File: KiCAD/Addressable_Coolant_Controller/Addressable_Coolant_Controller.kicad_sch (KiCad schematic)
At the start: 3 parts, among them J10 XW4M-12D2-H1DA, J11 XW4M-12D2-H1DA, J12 XW4M-02D1-H1DA

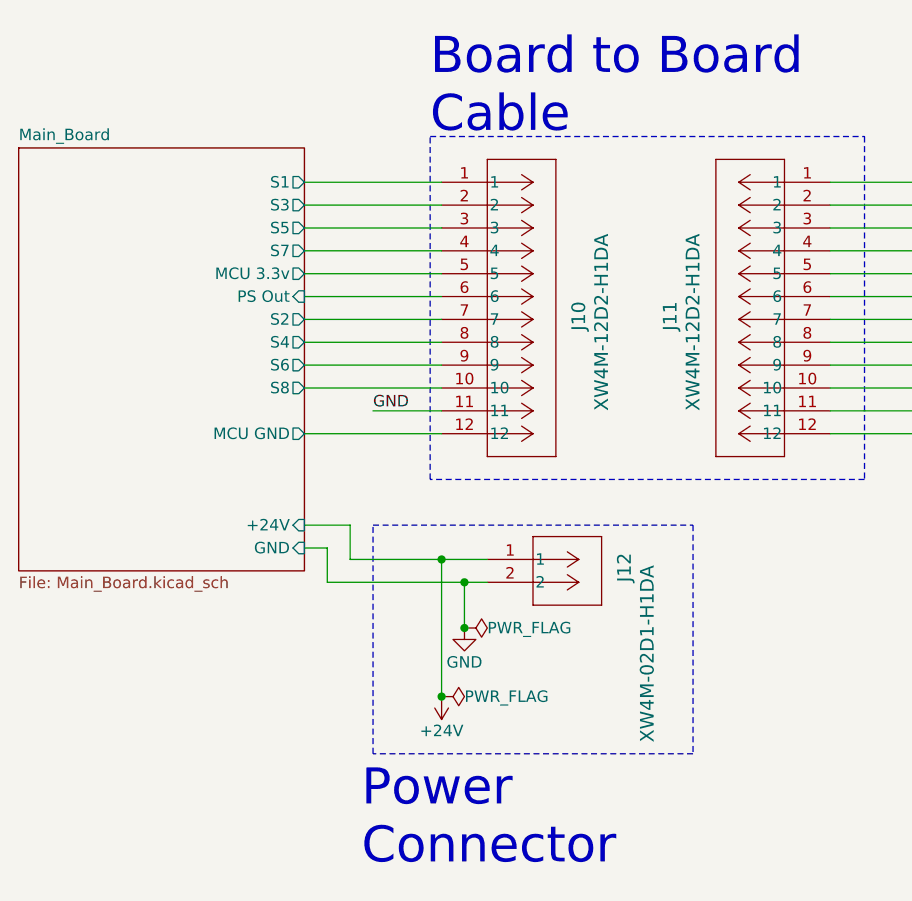
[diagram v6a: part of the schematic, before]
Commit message: Added LEDs to connector board, and moved to hierarchical sheet
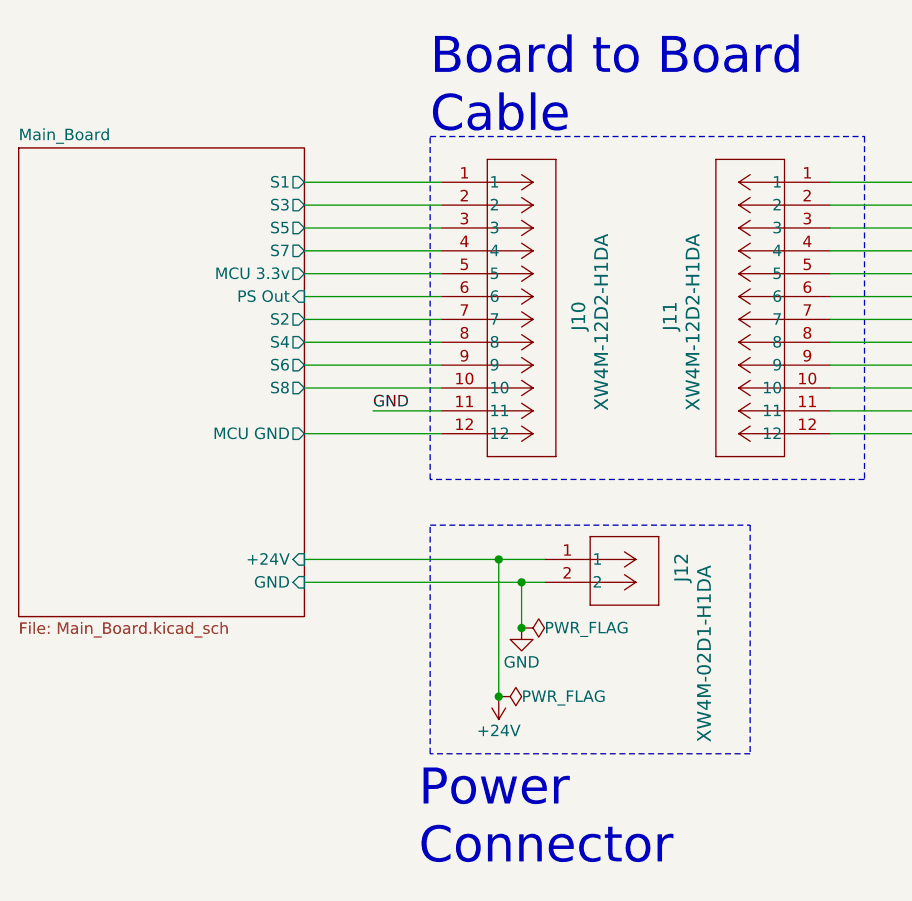
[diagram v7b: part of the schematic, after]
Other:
- moved on the sheet: J12
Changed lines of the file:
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@@
     (company "Warner Consulting Inc.")
   )
-  (junction (at 127 127) (diameter 0) (color 0 0 0 0)
-  )
-  (junction (at 129.54 114.3) (diameter 0) (color 0 0 0 0)
-  )
-  (junction (at 129.54 119.38) (diameter 0) (color 0 0 0 0)
-  )
-  (junction (at 127 111.76) (diameter 0) (color 0 0 0 0)
+  (junction (at 133.35 127) (diameter 0) (color 0 0 0 0)
+  )
+  (junction (at 135.89 114.3) (diameter 0) (color 0 0 0 0)
+  )
+  (junction (at 135.89 119.38) (diameter 0) (color 0 0 0 0)
+  )
+  (junction (at 133.35 111.76) (diameter 0) (color 0 0 0 0)
   )
   (wire (pts (xy 170.18 90.17) (xy 185.42 90.17))
@@
     (stroke (width 0) (type default))
   )
-  (wire (pts (xy 129.54 119.38) (xy 129.54 114.3))
-    (stroke (width 0) (type default))
-  )
-  (wire (pts (xy 127 111.76) (xy 132.08 111.76))
+  (wire (pts (xy 135.89 119.38) (xy 135.89 114.3))
+    (stroke (width 0) (type default))
+  )
+  (wire (pts (xy 133.35 111.76) (xy 138.43 111.76))
     (stroke (width 0) (type default))
   )
@@
     (stroke (width 0) (type default))
   )
-  (wire (pts (xy 116.84 111.76) (xy 116.84 107.95))
-    (stroke (width 0) (type default))
-  )
   (wire (pts (xy 170.18 69.85) (xy 185.42 69.85))
     (stroke (width 0) (type default))
@@
     (stroke (width 0) (type default))
   )
-  (wire (pts (xy 116.84 107.95) (xy 111.76 107.95))
+  (wire (pts (xy 111.76 111.76) (xy 133.35 111.76))
     (stroke (width 0) (type default))
   )
@@
     (stroke (width 0) (type default))
   )
-  (wire (pts (xy 111.76 110.49) (xy 114.3 110.49))
+  (wire (pts (xy 111.76 114.3) (xy 135.89 114.3))
     (stroke (width 0) (type default))
   )
@@
     (stroke (width 0) (type default))
   )
-  (wire (pts (xy 114.3 110.49) (xy 114.3 114.3))
-    (stroke (width 0) (type default))
-  )
   (wire (pts (xy 170.18 95.25) (xy 185.42 95.25))
     (stroke (width 0) (type default))
   )
-  (wire (pts (xy 116.84 111.76) (xy 127 111.76))
-    (stroke (width 0) (type default))
-  )
-  (wire (pts (xy 129.54 114.3) (xy 132.08 114.3))
+  (wire (pts (xy 135.89 114.3) (xy 138.43 114.3))
     (stroke (width 0) (type default))
   )
@@
     (stroke (width 0) (type default))
   )
-  (wire (pts (xy 114.3 114.3) (xy 129.54 114.3))
-    (stroke (width 0) (type default))
-  )
-  (wire (pts (xy 127 111.76) (xy 127 127))
+  (wire (pts (xy 133.35 111.76) (xy 133.35 127))
     (stroke (width 0) (type default))
   )
@@
     (stroke (width 0) (type default))
   )
-  (rectangle (start 119.38 107.95) (end 154.94 133.35)
+  (rectangle (start 125.73 107.95) (end 161.29 133.35)
     (stroke (width 0) (type dash_dot_dot))
     (fill (type none))
@@
     (effects (font (size 4 4)) (justify left bottom))
   )
-  (text "Power \nConnector" (at 118.11 146.05 0)
+  (text "Power \nConnector" (at 124.46 146.05 0)
     (effects (font (size 4 4)) (justify left bottom))
   )
@@
     (effects (font (size 1.27 1.27)) (justify left bottom))
   )
-  (symbol (lib_id "power:PWR_FLAG") (at 127 127 270) (unit 1)
+  (symbol (lib_id "power:PWR_FLAG") (at 133.35 127 270) (unit 1)
     (in_bom yes) (on_board yes) (dnp no)
-    (property "Reference" "#FLG01" (at 128.905 127 0)
+    (property "Reference" "#FLG01" (at 135.255 127 0)
       (effects (font (size 1.27 1.27)) hide)
     )
-    (property "Value" "PWR_FLAG" (at 129.54 127 90)
+    (property "Value" "PWR_FLAG" (at 135.89 127 90)
       (effects (font (size 1.27 1.27)) (justify left))
     )
-    (property "Footprint" "" (at 127 127 0)
+    (property "Footprint" "" (at 133.35 127 0)
       (effects (font (size 1.27 1.27)) hide)
     )
-    (property "Datasheet" "~" (at 127 127 0)
+    (property "Datasheet" "~" (at 133.35 127 0)
       (effects (font (size 1.27 1.27)) hide)
     )
@@
     )
   )
-  (symbol (lib_id "power:GND") (at 129.54 119.38 0) (unit 1)
+  (symbol (lib_id "power:GND") (at 135.89 119.38 0) (unit 1)
     (in_bom yes) (on_board yes) (dnp no)
-    (property "Reference" "#PWR02" (at 129.54 125.73 0)
+    (property "Reference" "#PWR02" (at 135.89 125.73 0)
       (effects (font (size 1.27 1.27)) hide)
     )
-    (property "Value" "GND" (at 129.54 123.19 0)
+    (property "Value" "GND" (at 135.89 123.19 0)
       (effects (font (size 1.27 1.27)))
     )
-    (property "Footprint" "" (at 129.54 119.38 0)
+    (property "Footprint" "" (at 135.89 119.38 0)
       (effects (font (size 1.27 1.27)) hide)
     )
-    (property "Datasheet" "" (at 129.54 119.38 0)
+    (property "Datasheet" "" (at 135.89 119.38 0)
       (effects (font (size 1.27 1.27)) hide)
     )
@@
     )
   )
-  (symbol (lib_id "xw4m-02d1-h1da:XW4M-02D1-H1DA") (at 132.08 111.76 0) (unit 1)
+  (symbol (lib_id "xw4m-02d1-h1da:XW4M-02D1-H1DA") (at 138.43 111.76 0) (unit 1)
     (in_bom yes) (on_board yes) (dnp no)
-    (property "Reference" "J12" (at 147.32 114.3 90)
+    (property "Reference" "J12" (at 153.67 114.3 90)
       (effects (font (size 1.524 1.524)) (justify left))
     )
-    (property "Value" "XW4M-02D1-H1DA" (at 149.86 132.08 90)
+    (property "Value" "XW4M-02D1-H1DA" (at 156.21 132.08 90)
       (effects (font (size 1.524 1.524)) (justify left))
     )
-    (property "Footprint" "xw4m-02d1-h1da:xw4m-02d1-h1da" (at 132.08 111.76 0)
+    (property "Footprint" "xw4m-02d1-h1da:xw4m-02d1-h1da" (at 138.43 111.76 0)
       (effects (font (size 1.27 1.27) italic) hide)
     )
-    (property "Datasheet" "XW4M-02D1-H1DA" (at 132.08 111.76 0)
+    (property "Datasheet" "XW4M-02D1-H1DA" (at 138.43 111.76 0)
       (effects (font (size 1.27 1.27) italic) hide)
     )
@@
     )
   )
-  (symbol (lib_id "power:PWR_FLAG") (at 129.54 119.38 270) (unit 1)
+  (symbol (lib_id "power:PWR_FLAG") (at 135.89 119.38 270) (unit 1)
     (in_bom yes) (on_board yes) (dnp no)
-    (property "Reference" "#FLG02" (at 131.445 119.38 0)
+    (property "Reference" "#FLG02" (at 137.795 119.38 0)
       (effects (font (size 1.27 1.27)) hide)
     )
-    (property "Value" "PWR_FLAG" (at 132.08 119.38 90)
+    (property "Value" "PWR_FLAG" (at 138.43 119.38 90)
       (effects (font (size 1.27 1.27)) (justify left))
     )
-    (property "Footprint" "" (at 129.54 119.38 0)
+    (property "Footprint" "" (at 135.89 119.38 0)
       (effects (font (size 1.27 1.27)) hide)
     )
-    (property "Datasheet" "~" (at 129.54 119.38 0)
+    (property "Datasheet" "~" (at 135.89 119.38 0)
       (effects (font (size 1.27 1.27)) hide)
     )
@@
     )
   )
-  (symbol (lib_id "power:+24V") (at 127 127 180) (unit 1)
+  (symbol (lib_id "power:+24V") (at 133.35 127 180) (unit 1)
     (in_bom yes) (on_board yes) (dnp no)
-    (property "Reference" "#PWR01" (at 127 123.19 0)
+    (property "Reference" "#PWR01" (at 133.35 123.19 0)
       (effects (font (size 1.27 1.27)) hide)
     )
-    (property "Value" "+24V" (at 127 130.81 0)
+    (property "Value" "+24V" (at 133.35 130.81 0)
       (effects (font (size 1.27 1.27)))
     )
-    (property "Footprint" "" (at 127 127 0)
+    (property "Footprint" "" (at 133.35 127 0)
       (effects (font (size 1.27 1.27)) hide)
     )
-    (property "Datasheet" "" (at 127 127 0)
+    (property "Datasheet" "" (at 133.35 127 0)
       (effects (font (size 1.27 1.27)) hide)
     )
@@
     )
   )
-  (sheet (at 80.01 66.04) (size 31.75 46.99) (fields_autoplaced)
+  (sheet (at 80.01 66.04) (size 31.75 52.07) (fields_autoplaced)
     (stroke (width 0.1524) (type solid))
     (fill (color 0 0 0 0.0000))
@@
       (effects (font (size 1.27 1.27)) (justify left bottom))
     )
-    (property "Sheetfile" "Main_Board.kicad_sch" (at 80.01 113.6146 0)
+    (property "Sheetfile" "Main_Board.kicad_sch" (at 80.01 118.6946 0)
       (effects (font (size 1.27 1.27)) (justify left top))
     )
@@
       (effects (font (size 1.27 1.27)) (justify right))
     )
-    (pin "+24V" input (at 111.76 107.95 0)
+    (pin "+24V" input (at 111.76 111.76 0)
       (effects (font (size 1.27 1.27)) (justify right))
     )
-    (pin "GND" input (at 111.76 110.49 0)
+    (pin "GND" input (at 111.76 114.3 0)
       (effects (font (size 1.27 1.27)) (justify right))
     )
